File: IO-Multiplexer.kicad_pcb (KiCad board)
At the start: 2 copper layers, 68.6 x 129.5 mm, 19 parts

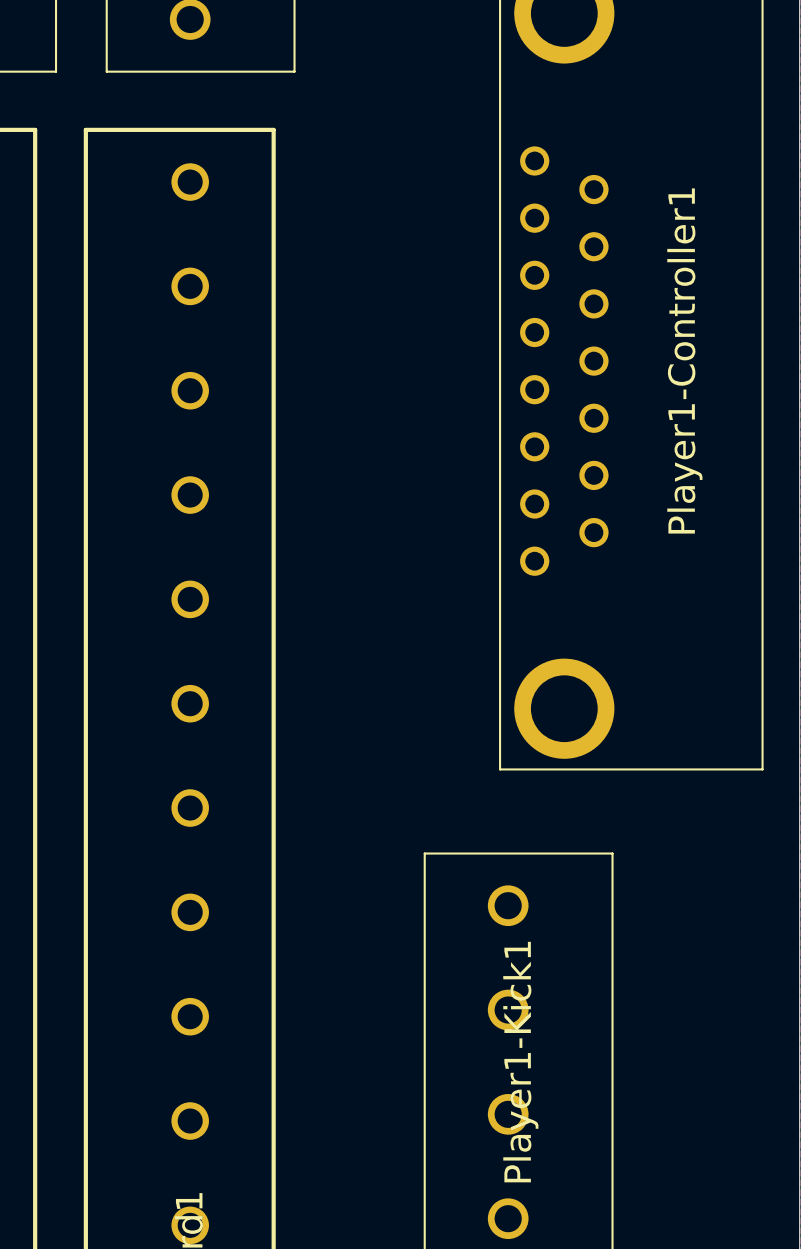
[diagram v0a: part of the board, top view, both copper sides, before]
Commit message: Fully routed P1 controls
Making more efficient use of traces
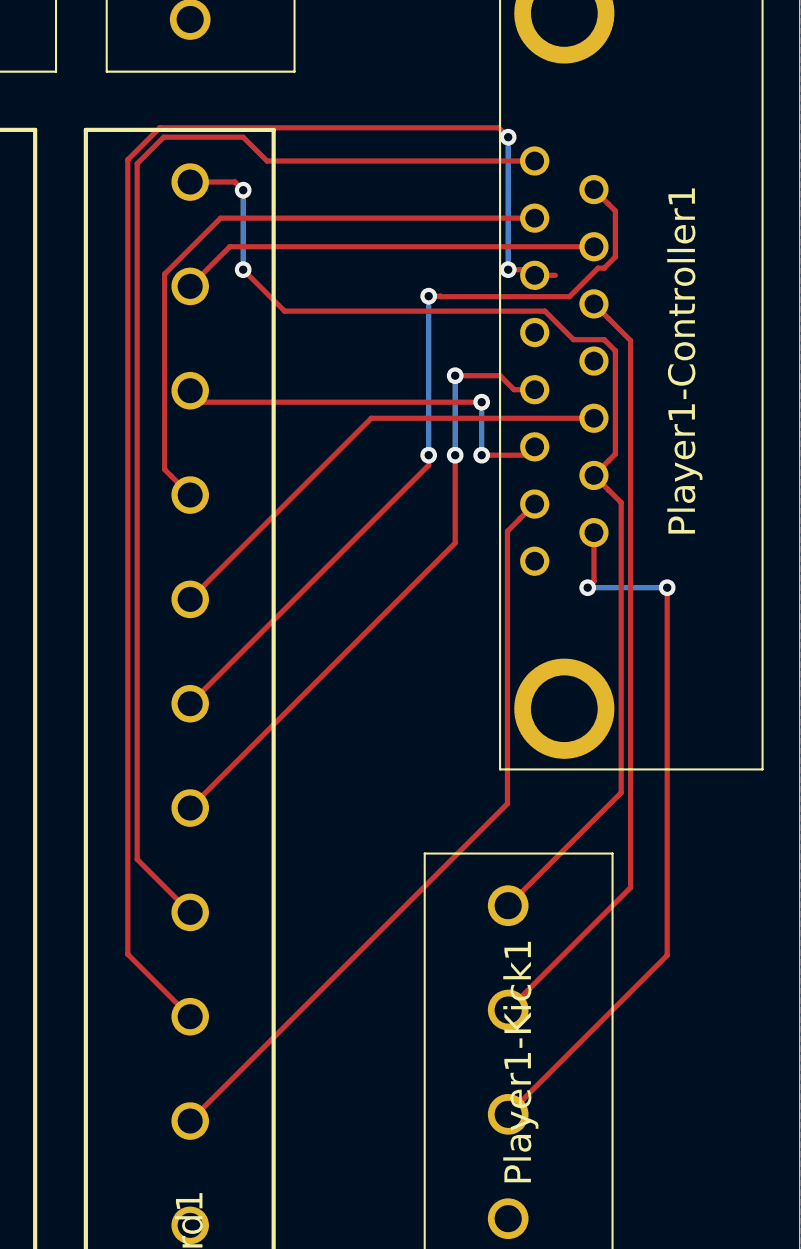
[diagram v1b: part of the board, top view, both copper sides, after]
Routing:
- net /P1-Start: track 0.00 -> 70.1 mm, vias 0 -> 2
- net /P1-Up: track 0.00 -> 57.0 mm
- net /P1-Button4: track 0.00 -> 55.8 mm, vias 0 -> 2
- net /P1-Left: track 0.00 -> 37.7 mm, vias 0 -> 2
- net /P1-Button5: track 0.00 -> 37.0 mm
- net /P1-Coin: track 0.00 -> 36.4 mm
- net /P1-Button6: track 0.00 -> 35.0 mm, vias 0 -> 2
- net /P1-Down: track 0.00 -> 30.1 mm, vias 0 -> 2
- net /P1-Button1: track 0.00 -> 29.9 mm
- net /P1-Right: track 0.00 -> 22.9 mm
- net /P1-Button3: track 0.00 -> 20.1 mm
- net /P1-Button2: track 0.00 -> 19.4 mm, vias 0 -> 2
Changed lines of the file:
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@@
     (thickness 1.6)
     (drawings 4)
-    (tracks 12)
+    (tracks 100)
     (zones 0)
     (modules 19)
@@
   )
   (setup
-    (last_trace_width 0.499872)
+    (last_trace_width 0.25)
     (user_trace_width 0.499872)
     (trace_clearance 0.2)
@@
     (solder_mask_min_width 0.25)
     (aux_axis_origin 0 0)
-    (visible_elements FFFFFF7F)
+    (visible_elements 7FFFFFFF)
     (pcbplotparams
       (layerselection 0x010fc_ffffffff)
@@
   (gr_line (start 207.01 13.97) (end 207.01 143.51) (layer Edge.Cuts) (width 0.05))
   (gr_line (start 138.43 13.97) (end 207.01 13.97) (layer Edge.Cuts) (width 0.05))
+  (via (at 189.23 67.31) (size 0.8) (drill 0.4) (layers F.Cu B.Cu) (net 22))
+  (via (at 191.77 72.39) (size 0.8) (drill 0.4) (layers F.Cu B.Cu) (net 15))
+  (via (at 191.77 74.93) (size 0.8) (drill 0.4) (layers F.Cu B.Cu) (net 15))
+  (via (at 193.04 66.04) (size 0.8) (drill 0.4) (layers F.Cu B.Cu) (net 19))
   (segment (start 179.07 139.7) (end 193.04 139.7) (width 0.25) (layer B.Cu) (net 1))
   (segment (start 179.07 134.7) (end 193.04 134.7) (width 0.25) (layer B.Cu) (net 2))
   (segment (start 179.07 129.7) (end 193.04 129.7) (width 0.25) (layer B.Cu) (net 3))
   (segment (start 179.07 124.7) (end 193.04 124.7) (width 0.25) (layer B.Cu) (net 4))
+  (via (at 189.23 74.93) (size 0.8) (drill 0.4) (layers F.Cu B.Cu) (net 22))
+  (via (at 180.34 62.23) (size 0.8) (drill 0.4) (layers F.Cu B.Cu) (net 14))
+  (via (at 190.5 74.93) (size 0.8) (drill 0.4) (layers F.Cu B.Cu) (net 17))
   (segment (start 161.21 134.54) (end 166.37 139.7) (width 0.499872) (layer B.Cu) (net 7))
   (segment (start 152.4 134.54) (end 161.21 134.54) (width 0.499872) (layer B.Cu) (net 7))
   (segment (start 161.21 129.54) (end 166.37 134.7) (width 0.499872) (layer B.Cu) (net 8))
   (segment (start 152.4 129.54) (end 161.21 129.54) (width 0.499872) (layer B.Cu) (net 8))
+  (via (at 180.34 66.04) (size 0.8) (drill 0.4) (layers F.Cu B.Cu) (net 14))
+  (via (at 190.5 71.12) (size 0.8) (drill 0.4) (layers F.Cu B.Cu) (net 17))
+  (via (at 193.04 59.69) (size 0.8) (drill 0.4) (layers F.Cu B.Cu) (net 19))
+  (via (at 196.85 81.28) (size 0.8) (drill 0.4) (layers F.Cu B.Cu) (net 12))
+  (via (at 200.66 81.28) (size 0.8) (drill 0.4) (layers F.Cu B.Cu) (net 12))
   (segment (start 167.16 39.05) (end 177.8 39.05) (width 0.499872) (layer F.Cu) (net 10))
   (segment (start 152.4 24.29) (end 167.16 39.05) (width 0.499872) (layer F.Cu) (net 10))
   (segment (start 167.16 44.05) (end 177.8 44.05) (width 0.499872) (layer F.Cu) (net 11))
   (segment (start 152.4 29.29) (end 167.16 44.05) (width 0.499872) (layer F.Cu) (net 11))
+  (segment (start 197.15 80.98) (end 196.85 81.28) (width 0.25) (layer F.Cu) (net 12))
+  (segment (start 197.15 78.64) (end 197.15 80.98) (width 0.25) (layer F.Cu) (net 12))
+  (segment (start 196.85 81.28) (end 200.66 81.28) (width 0.25) (layer B.Cu) (net 12))
+  (segment (start 200.66 98.9) (end 193.04 106.52) (width 0.25) (layer F.Cu) (net 12))
+  (segment (start 200.66 81.28) (end 200.66 98.9) (width 0.25) (layer F.Cu) (net 12))
+  (segment (start 193.610001 77.969999) (end 194.31 77.27) (width 0.25) (layer F.Cu) (net 13))
+  (segment (start 193.004999 78.575001) (end 193.610001 77.969999) (width 0.25) (layer F.Cu) (net 13))
+  (segment (start 193.004999 91.635001) (end 193.004999 78.575001) (width 0.25) (layer F.Cu) (net 13))
+  (segment (start 177.8 106.84) (end 193.004999 91.635001) (width 0.25) (layer F.Cu) (net 13))
+  (segment (start 197.849999 76.599999) (end 197.15 75.9) (width 0.25) (layer F.Cu) (net 14))
+  (segment (start 198.455001 91.104999) (end 198.455001 77.205001) (width 0.25) (layer F.Cu) (net 14))
+  (segment (start 198.455001 77.205001) (end 197.849999 76.599999) (width 0.25) (layer F.Cu) (net 14))
+  (segment (start 193.04 96.52) (end 198.455001 91.104999) (width 0.25) (layer F.Cu) (net 14))
+  (segment (start 179.95 61.84) (end 180.34 62.23) (width 0.25) (layer F.Cu) (net 14))
+  (segment (start 177.8 61.84) (end 179.95 61.84) (width 0.25) (layer F.Cu) (net 14))
+  (segment (start 180.34 62.23) (end 180.34 66.04) (width 0.25) (layer B.Cu) (net 14))
+  (segment (start 197.849999 75.200001) (end 197.15 75.9) (width 0.25) (layer F.Cu) (net 14))
+  (segment (start 198.175001 69.927999) (end 198.175001 74.874999) (width 0.25) (layer F.Cu) (net 14))
+  (segment (start 196.172001 69.394999) (end 197.642001 69.394999) (width 0.25) (layer F.Cu) (net 14))
+  (segment (start 198.175001 74.874999) (end 197.849999 75.200001) (width 0.25) (layer F.Cu) (net 14))
+  (segment (start 194.802001 68.024999) (end 196.172001 69.394999) (width 0.25) (layer F.Cu) (net 14))
+  (segment (start 182.324999 68.024999) (end 194.802001 68.024999) (width 0.25) (layer F.Cu) (net 14))
+  (segment (start 197.642001 69.394999) (end 198.175001 69.927999) (width 0.25) (layer F.Cu) (net 14))
+  (segment (start 180.34 66.04) (end 182.324999 68.024999) (width 0.25) (layer F.Cu) (net 14))
+  (segment (start 193.91 74.93) (end 194.31 74.53) (width 0.25) (layer F.Cu) (net 15))
+  (segment (start 191.77 74.93) (end 193.91 74.93) (width 0.25) (layer F.Cu) (net 15))
+  (segment (start 178.35 72.39) (end 177.8 71.84) (width 0.25) (layer F.Cu) (net 15))
+  (segment (start 191.77 72.39) (end 178.35 72.39) (width 0.25) (layer F.Cu) (net 15))
+  (segment (start 191.77 72.39) (end 191.77 74.93) (width 0.25) (layer B.Cu) (net 15))
+  (segment (start 186.48 73.16) (end 177.8 81.84) (width 0.25) (layer F.Cu) (net 16))
+  (segment (start 197.15 73.16) (end 186.48 73.16) (width 0.25) (layer F.Cu) (net 16))
+  (segment (start 191.065685 71.12) (end 190.5 71.12) (width 0.25) (layer F.Cu) (net 17))
+  (segment (start 192.650051 71.12) (end 191.065685 71.12) (width 0.25) (layer F.Cu) (net 17))
+  (segment (start 193.320051 71.79) (end 192.650051 71.12) (width 0.25) (layer F.Cu) (net 17))
+  (segment (start 194.31 71.79) (end 193.320051 71.79) (width 0.25) (layer F.Cu) (net 17))
+  (segment (start 190.5 71.12) (end 190.5 74.93) (width 0.25) (layer B.Cu) (net 17))
+  (segment (start 190.5 79.14) (end 190.5 74.93) (width 0.25) (layer F.Cu) (net 17))
+  (segment (start 177.8 91.84) (end 190.5 79.14) (width 0.25) (layer F.Cu) (net 17))
+  (segment (start 197.849999 68.379999) (end 197.15 67.68) (width 0.25) (layer F.Cu) (net 18))
+  (segment (start 198.90501 69.43501) (end 197.849999 68.379999) (width 0.25) (layer F.Cu) (net 18))
+  (segment (start 198.90501 95.65499) (end 198.90501 69.43501) (width 0.25) (layer F.Cu) (net 18))
+  (segment (start 193.04 101.52) (end 198.90501 95.65499) (width 0.25) (layer F.Cu) (net 18))
+  (segment (start 195.299949 66.31) (end 194.31 66.31) (width 0.25) (layer F.Cu) (net 19))
+  (segment (start 174.809991 60.773599) (end 176.3436 59.23999) (width 0.25) (layer F.Cu) (net 19))
+  (segment (start 174.809991 98.849991) (end 174.809991 60.773599) (width 0.25) (layer F.Cu) (net 19))
+  (segment (start 177.8 101.84) (end 174.809991 98.849991) (width 0.25) (layer F.Cu) (net 19))
+  (segment (start 193.04 66.04) (end 193.04 59.69) (width 0.25) (layer B.Cu) (net 19))
+  (segment (start 194.04 66.04) (end 194.31 66.31) (width 0.25) (layer F.Cu) (net 19))
+  (segment (start 193.04 66.04) (end 194.04 66.04) (width 0.25) (layer F.Cu) (net 19))
+  (segment (start 192.58999 59.23999) (end 193.04 59.69) (width 0.25) (layer F.Cu) (net 19))
+  (segment (start 176.3436 59.23999) (end 192.58999 59.23999) (width 0.25) (layer F.Cu) (net 19))
+  (segment (start 179.7 64.94) (end 177.8 66.84) (width 0.25) (layer F.Cu) (net 20))
+  (segment (start 197.15 64.94) (end 179.7 64.94) (width 0.25) (layer F.Cu) (net 20))
+  (segment (start 176.900001 75.940001) (end 177.8 76.84) (width 0.25) (layer F.Cu) (net 21))
+  (segment (start 176.574999 75.614999) (end 176.900001 75.940001) (width 0.25) (layer F.Cu) (net 21))
+  (segment (start 176.574999 66.251999) (end 176.574999 75.614999) (width 0.25) (layer F.Cu) (net 21))
+  (segment (start 179.256998 63.57) (end 176.574999 66.251999) (width 0.25) (layer F.Cu) (net 21))
+  (segment (start 194.31 63.57) (end 179.256998 63.57) (width 0.25) (layer F.Cu) (net 21))
+  (segment (start 189.23 75.41) (end 189.23 74.93) (width 0.25) (layer F.Cu) (net 22))
+  (segment (start 177.8 86.84) (end 189.23 75.41) (width 0.25) (layer F.Cu) (net 22))
+  (segment (start 197.849999 62.899999) (end 197.15 62.2) (width 0.25) (layer F.Cu) (net 22))
+  (segment (start 197.642001 65.965001) (end 198.175001 65.432001) (width 0.25) (layer F.Cu) (net 22))
+  (segment (start 197.347997 65.965001) (end 197.642001 65.965001) (width 0.25) (layer F.Cu) (net 22))
+  (segment (start 198.175001 63.225001) (end 197.849999 62.899999) (width 0.25) (layer F.Cu) (net 22))
+  (segment (start 198.175001 65.432001) (end 198.175001 63.225001) (width 0.25) (layer F.Cu) (net 22))
+  (segment (start 195.977997 67.335001) (end 197.347997 65.965001) (width 0.25) (layer F.Cu) (net 22))
+  (segment (start 189.820686 67.335001) (end 195.977997 67.335001) (width 0.25) (layer F.Cu) (net 22))
+  (segment (start 189.795685 67.31) (end 189.820686 67.335001) (width 0.25) (layer F.Cu) (net 22))
+  (segment (start 189.23 67.31) (end 189.795685 67.31) (width 0.25) (layer F.Cu) (net 22))
+  (segment (start 189.23 74.93) (end 189.23 67.31) (width 0.25) (layer B.Cu) (net 22))
+  (segment (start 194.31 60.83) (end 181.48 60.83) (width 0.25) (layer F.Cu) (net 23))
+  (segment (start 181.48 60.83) (end 180.34 59.69) (width 0.25) (layer F.Cu) (net 23))
+  (segment (start 180.34 59.69) (end 176.53 59.69) (width 0.25) (layer F.Cu) (net 23))
+  (segment (start 176.53 59.69) (end 175.26 60.96) (width 0.25) (layer F.Cu) (net 23))
+  (segment (start 175.26 94.3) (end 177.8 96.84) (width 0.25) (layer F.Cu) (net 23))
+  (segment (start 175.26 60.96) (end 175.26 94.3) (width 0.25) (layer F.Cu) (net 23))
   (zone (net 9) (net_name /+5V) (layer F.Cu) (hatch edge 0.508)
     (connect_pads (clearance 0.508))

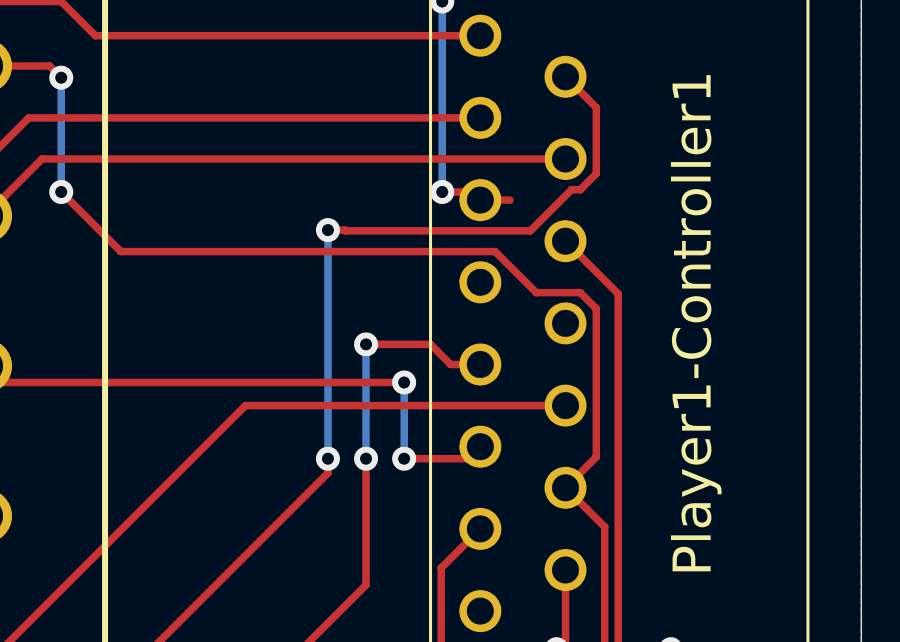
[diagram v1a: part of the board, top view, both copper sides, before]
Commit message: Fix a DRC error, via too close to track
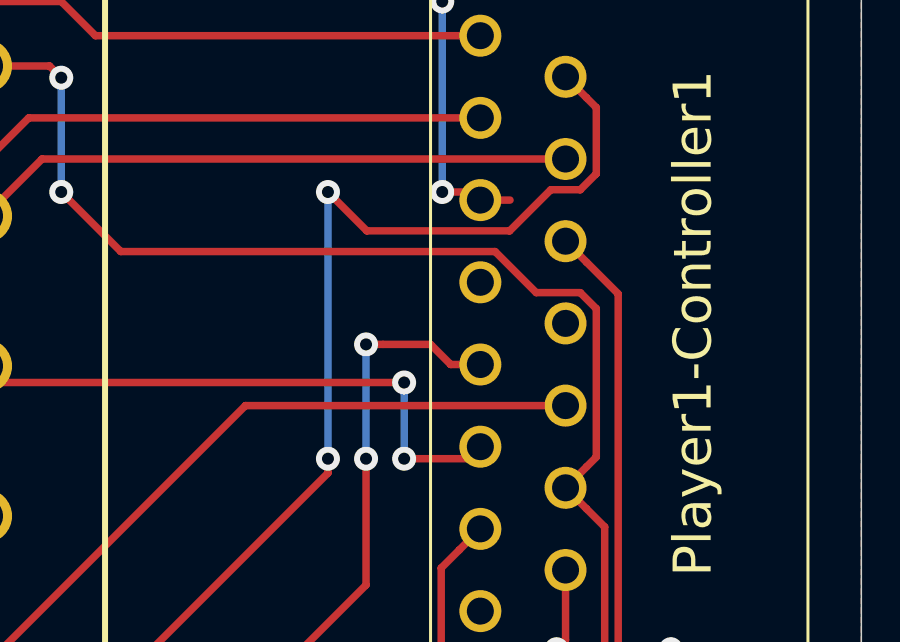
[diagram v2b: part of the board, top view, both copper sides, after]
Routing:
- net /P1-Left: track 37.7 -> 39.5 mm
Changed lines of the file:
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@@
     (thickness 1.6)
     (drawings 4)
-    (tracks 100)
+    (tracks 99)
     (zones 0)
     (modules 19)
@@
   (gr_line (start 207.01 13.97) (end 207.01 143.51) (layer Edge.Cuts) (width 0.05))
   (gr_line (start 138.43 13.97) (end 207.01 13.97) (layer Edge.Cuts) (width 0.05))
-  (via (at 189.23 67.31) (size 0.8) (drill 0.4) (layers F.Cu B.Cu) (net 22))
+  (via (at 189.23 66.04) (size 0.8) (drill 0.4) (layers F.Cu B.Cu) (net 22))
   (via (at 191.77 72.39) (size 0.8) (drill 0.4) (layers F.Cu B.Cu) (net 15))
   (via (at 191.77 74.93) (size 0.8) (drill 0.4) (layers F.Cu B.Cu) (net 15))
@@
   (segment (start 179.07 129.7) (end 193.04 129.7) (width 0.25) (layer B.Cu) (net 3))
   (segment (start 179.07 124.7) (end 193.04 124.7) (width 0.25) (layer B.Cu) (net 4))
-  (via (at 189.23 74.93) (size 0.8) (drill 0.4) (layers F.Cu B.Cu) (net 22))
   (via (at 180.34 62.23) (size 0.8) (drill 0.4) (layers F.Cu B.Cu) (net 14))
   (via (at 190.5 74.93) (size 0.8) (drill 0.4) (layers F.Cu B.Cu) (net 17))
@@
   (segment (start 179.256998 63.57) (end 176.574999 66.251999) (width 0.25) (layer F.Cu) (net 21))
   (segment (start 194.31 63.57) (end 179.256998 63.57) (width 0.25) (layer F.Cu) (net 21))
+  (via (at 189.23 74.93) (size 0.8) (drill 0.4) (layers F.Cu B.Cu) (net 22))
   (segment (start 189.23 75.41) (end 189.23 74.93) (width 0.25) (layer F.Cu) (net 22))
   (segment (start 177.8 86.84) (end 189.23 75.41) (width 0.25) (layer F.Cu) (net 22))
+  (segment (start 189.23 66.04) (end 189.23 74.93) (width 0.25) (layer B.Cu) (net 22))
   (segment (start 197.849999 62.899999) (end 197.15 62.2) (width 0.25) (layer F.Cu) (net 22))
-  (segment (start 197.642001 65.965001) (end 198.175001 65.432001) (width 0.25) (layer F.Cu) (net 22))
-  (segment (start 197.347997 65.965001) (end 197.642001 65.965001) (width 0.25) (layer F.Cu) (net 22))
   (segment (start 198.175001 63.225001) (end 197.849999 62.899999) (width 0.25) (layer F.Cu) (net 22))
   (segment (start 198.175001 65.432001) (end 198.175001 63.225001) (width 0.25) (layer F.Cu) (net 22))
-  (segment (start 195.977997 67.335001) (end 197.347997 65.965001) (width 0.25) (layer F.Cu) (net 22))
-  (segment (start 189.820686 67.335001) (end 195.977997 67.335001) (width 0.25) (layer F.Cu) (net 22))
-  (segment (start 189.795685 67.31) (end 189.820686 67.335001) (width 0.25) (layer F.Cu) (net 22))
-  (segment (start 189.23 67.31) (end 189.795685 67.31) (width 0.25) (layer F.Cu) (net 22))
-  (segment (start 189.23 74.93) (end 189.23 67.31) (width 0.25) (layer B.Cu) (net 22))
+  (segment (start 197.642001 65.965001) (end 198.175001 65.432001) (width 0.25) (layer F.Cu) (net 22))
+  (segment (start 195.287999 67.335001) (end 196.657999 65.965001) (width 0.25) (layer F.Cu) (net 22))
+  (segment (start 190.525001 67.335001) (end 195.287999 67.335001) (width 0.25) (layer F.Cu) (net 22))
+  (segment (start 196.657999 65.965001) (end 197.642001 65.965001) (width 0.25) (layer F.Cu) (net 22))
+  (segment (start 189.23 66.04) (end 190.525001 67.335001) (width 0.25) (layer F.Cu) (net 22))
   (segment (start 194.31 60.83) (end 181.48 60.83) (width 0.25) (layer F.Cu) (net 23))
   (segment (start 181.48 60.83) (end 180.34 59.69) (width 0.25) (layer F.Cu) (net 23))
